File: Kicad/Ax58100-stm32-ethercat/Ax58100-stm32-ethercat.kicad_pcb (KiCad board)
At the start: 2 copper layers, 94.5 x 74.4 mm, 183 parts, among them J1 Step1, J10 Encoder, J11 5V Power IN, J12 24V Field, J13 DAC, J14 In_opt1, J15 Serial usart1, J16 In_opt2, J17 STLINK, J18 Out_opt, J2 Step2, J3 Step3, J4 Step4, J5 THCAD, J6 In1-4, J7 In5-8, J8 Output1-2, J9 Output3-4, SW1 SW PB, U1 MAX3485CSA/ESA, U10 AX58100, U2 TXS0108EPW, U3 TLP292-4, U4 TLP292-4, U5 TLP292-4, U6 STM32F407VGT6, U7 AMS1117-3.3, U8 24LC32A, U9 AMS1117-1.2, Y1 8 MHz, Y2 NXK25.000AE12F-KAB6-12

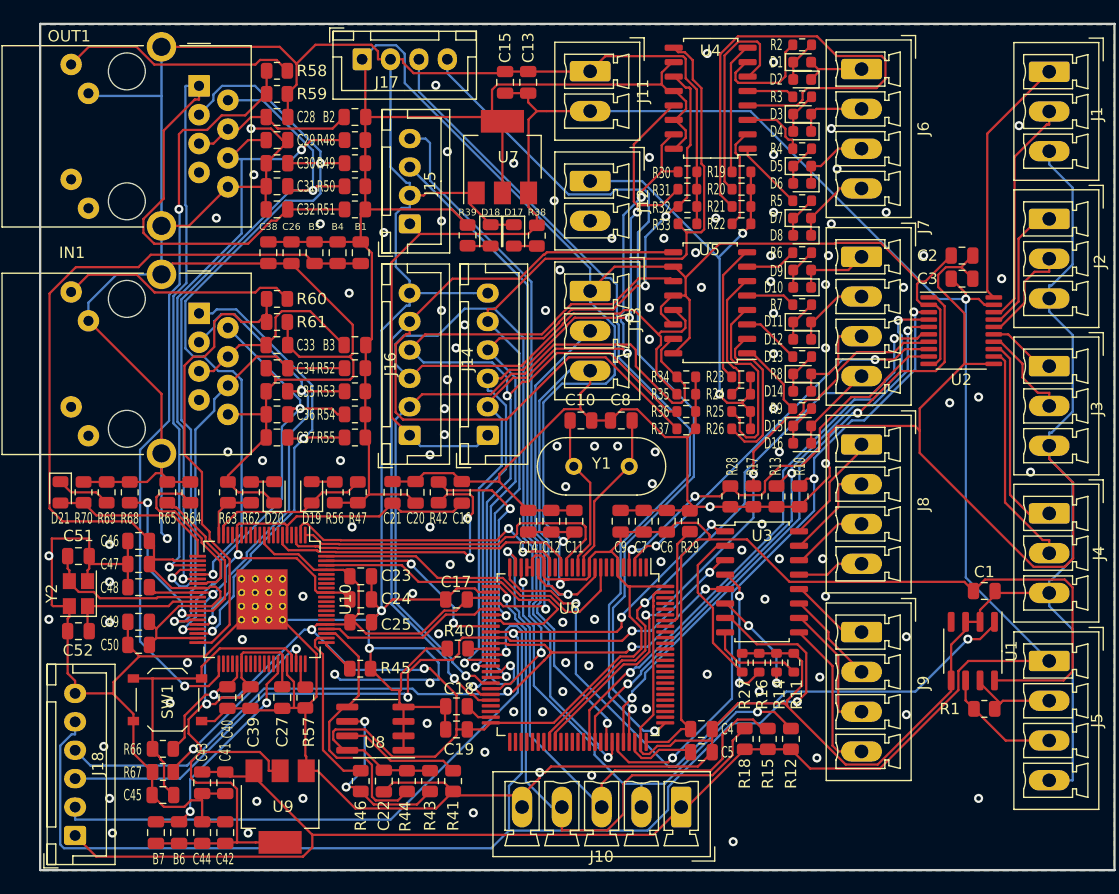
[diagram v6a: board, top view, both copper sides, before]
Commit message: 4.7k to 4k7
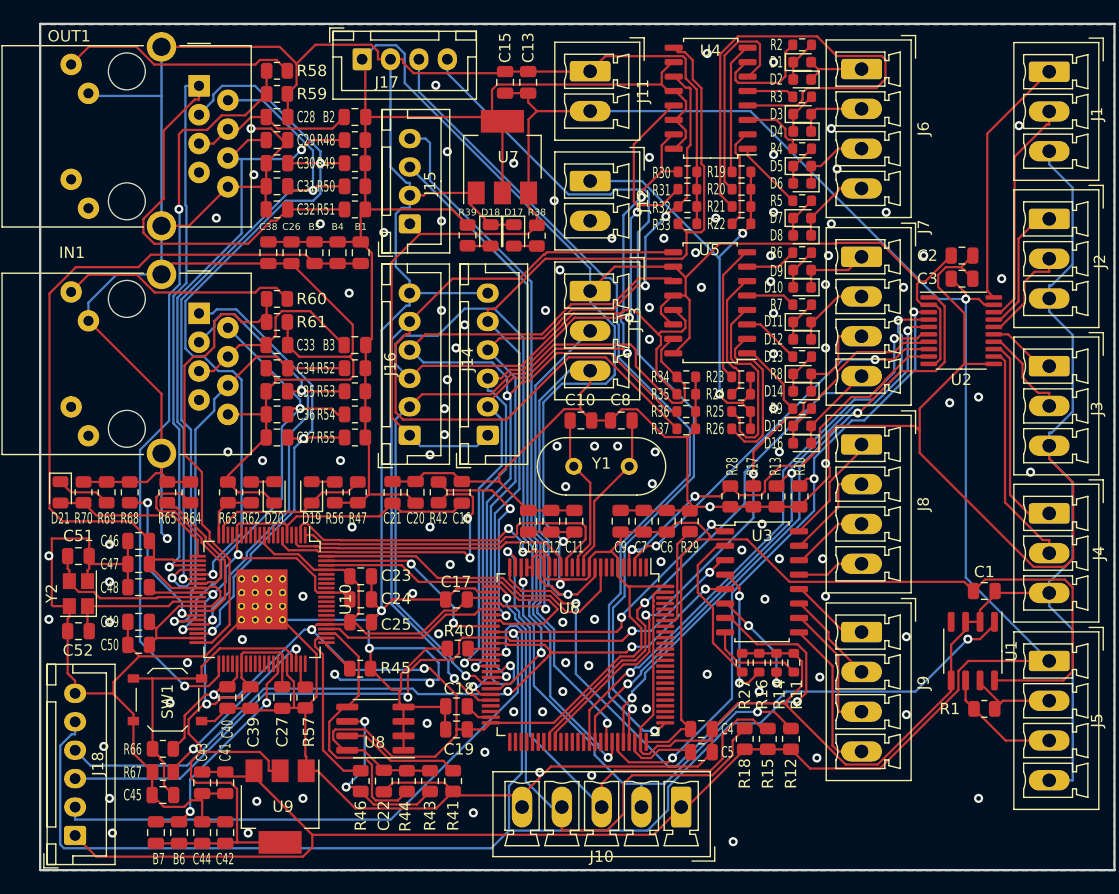
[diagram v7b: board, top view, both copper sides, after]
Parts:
- R41, R43, R44, R45, R47, R63, R64, R66, R67, R68, R70: value 4.7k -> 4k7
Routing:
- net GND: track 841.0 -> 816.0 mm
- net +3.3V: track 463.8 -> 454.9 mm
- net Net-(J9-Pin_1): track 7.07 -> 5.35 mm
- net +5V: track 247.1 -> 245.5 mm
- net STEP2_DIR_OUT: track 11.8 -> 10.2 mm
- net STEP3_DIR_OUT: track 6.04 -> 5.23 mm
- net Net-(R27-Pad1): track 14.1 -> 13.4 mm
- net IO5: track 64.6 -> 63.9 mm
- net STEP1_DIR: track 53.9 -> 53.2 mm
- net STEP1_STEP_OUT: track 20.2 -> 19.6 mm
- net STEP4_DIR_OUT: track 17.9 -> 17.3 mm
- net STEP2_STEP_OUT: track 9.13 -> 8.54 mm
- net STEP3_STEP_OUT: track 8.60 -> 8.01 mm
- net IO1: track 75.6 -> 75.0 mm
- net STEP4_STEP_OUT: track 20.0 -> 19.4 mm
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
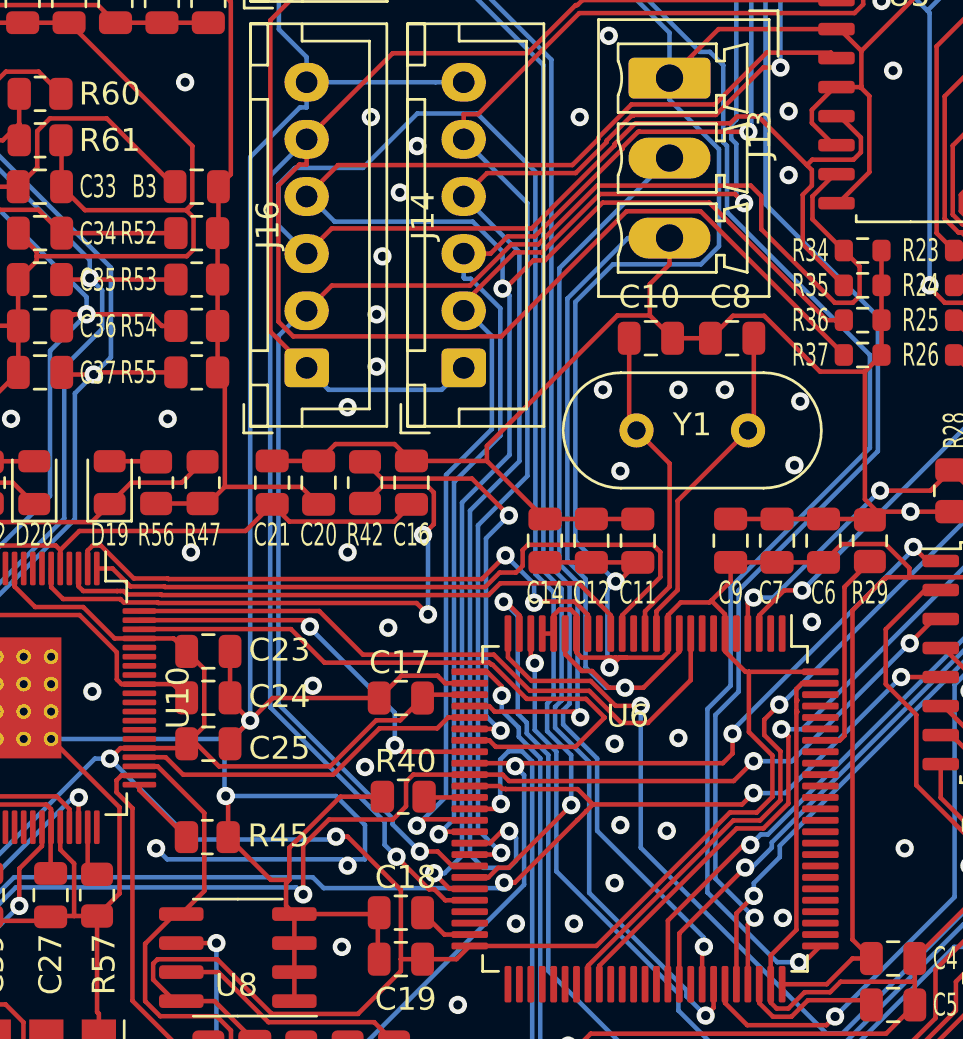
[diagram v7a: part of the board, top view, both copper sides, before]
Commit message: Added 4k7 pullup onm scs_func. Think not needed since it is to a pin on stm32, but in case
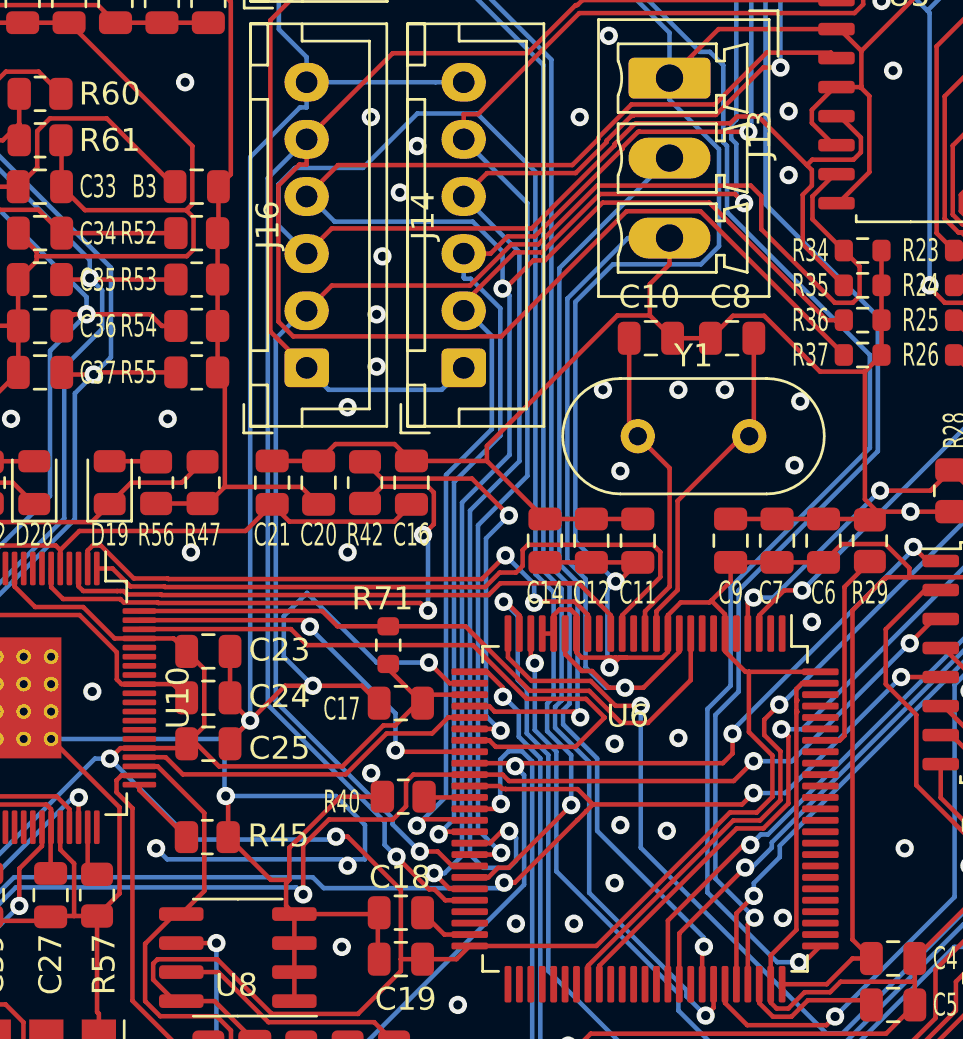
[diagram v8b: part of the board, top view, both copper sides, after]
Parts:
- added R71: 4k7, Resistor_SMD:R_0603_1608Metric, F.Cu at (122.2, 98.3)
- Y1: footprint Crystal:Crystal_HC49-U_Vertical -> Crystal:Crystal_HC49-4H_Vertical
- moved Y1 0.26 mm to (133.1, 89.2)
- moved C17 0.22 mm to (122.7, 100.8)
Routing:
- net GND: track 816.0 -> 825.8 mm
- net +3.3V: track 454.9 -> 457.7 mm
- net Net-(U6-PH0): track 14.3 -> 14.9 mm
